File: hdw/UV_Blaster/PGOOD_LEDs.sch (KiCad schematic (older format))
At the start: 14 parts

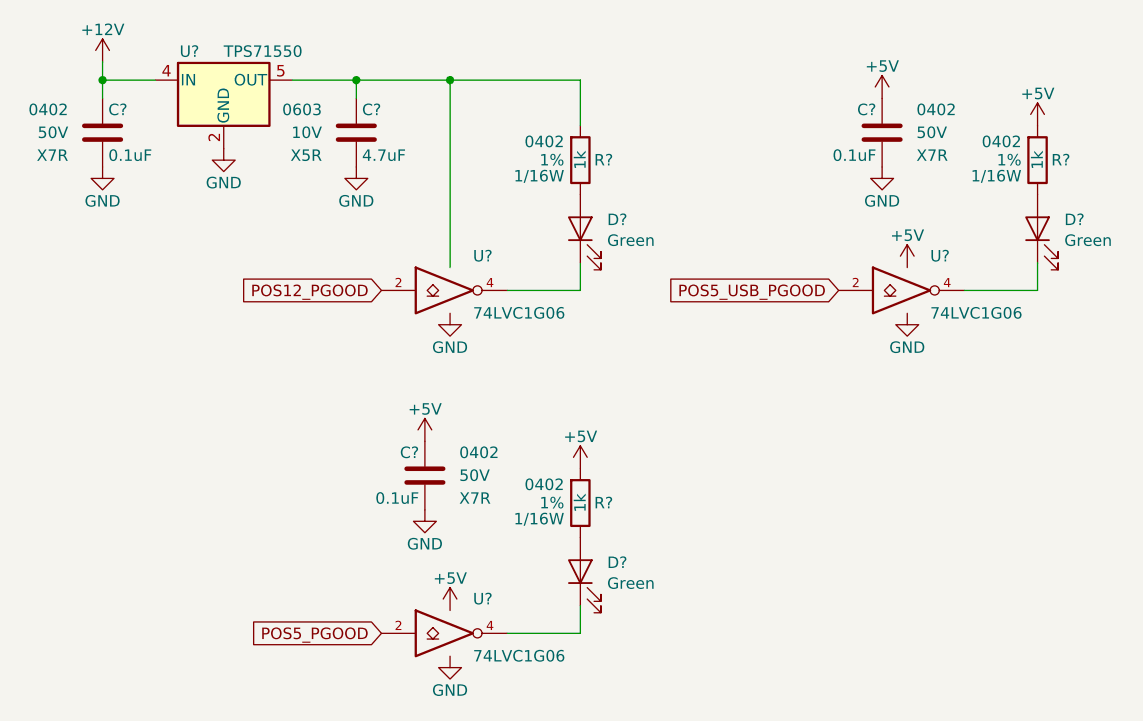
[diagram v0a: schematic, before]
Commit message: More sch work, netlist, part numbers, footprints
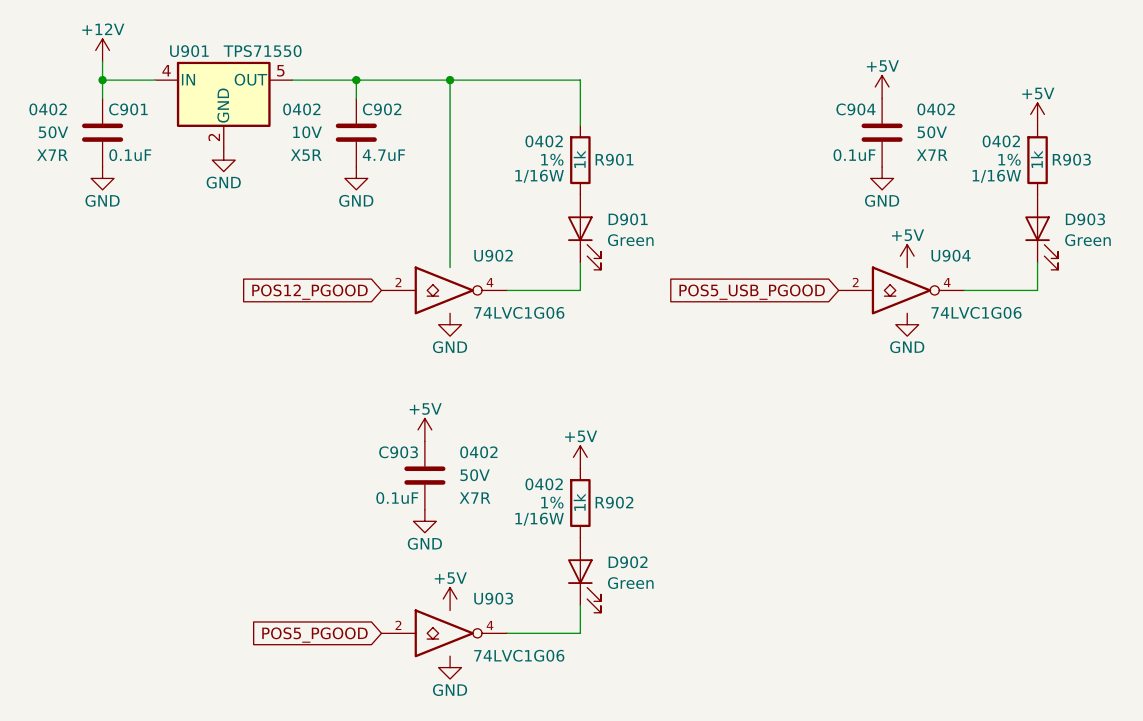
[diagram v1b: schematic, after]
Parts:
- C902: renamed from C?; footprint Capacitors_SMD:C_0603 -> Capacitors_SMD:C_0402; Digi-Key PN 490-16348-1-ND -> 490-14306-1-ND; display_footprint 0603 -> 0402
- D901, D902, D903: renamed from D?; footprint (none) -> LEDs:LED_0402; Digi-Key PN (none) -> 754-1815-1-ND
- R901, R902, R903: renamed from R?; Digi-Key PN 541-1.00KLCT-ND -> P1.00KLCT-ND
- U901: renamed from U?; Digi-Key PN (none) -> 296-15046-1-ND
- gave numbers to parts that had none: 6
